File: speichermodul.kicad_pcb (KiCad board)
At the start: 2 copper layers, 100 x 160 mm, 65 parts, among them IC1 6116, P1 CONN_3X2, P2 CONN_01X01, P3 CONN_01X01, P4 CONN_01X01, P5 CONN_01X01, P6 CONN_01X01, P7 CONN_01X01, P8 CONN_02X10, P9 CONN_02X10, SW1 SW_PUSH, SW2 SW_PUSH, U1 7400, U2 74LS08, U3 74LS08, U4 74LS14, U5 74LS540, U6 74LS540

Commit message: mit Korrektur der Anordnung begonnen
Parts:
- removed REF**: EuroBoard160mmX100mm, EuroBoard_Outline:EuroBoard160mmX100mm
- removed REF***: KiCad-Logo2_30mm_SilkScreen, Symbols:KiCad-Logo2_30mm_SilkScreen
- removed RP3: R_PACK8BUSSED, Housings_SIP:SIP9_Housing_BigPads
- added RP2: R_PACK8BUSSED, Housings_SIP:SIP9_Housing_BigPads, F.Cu at (72.6, 66.8)
- D1, D2: footprint LEDs:LED-3MM -> LEDs:LED_D3.0mm
- P8: footprint Connect:IDC_Header_Straight_20pins -> Connectors_Samtec:SDL-120-X-XX_2x10
- R24, R25, R3: footprint Resistors_ThroughHole:R_Axial_DIN0207_L6.3mm_D2.5mm_P10.16mm_Horizontal -> Resistors_ThroughHole:R_Axial_DIN0309_L9.0mm_D3.2mm_P15.24mm_Horizontal
- SW1, SW2: footprint Buttons_Switches_ThroughHole:SW_PUSH_6mm_h5mm -> tg_foodprint:SW_PUSH_LCD_E3_SAxxxx_tg
- U5: footprint Housings_DIP:DIP-20_W7.62mm_LongPads -> Housings_DIP:DIP-20_W7.62mm_Socket_LongPads
- moved D18 104.1 mm to (57.1, 29.2)
- moved U5 99.1 mm to (64.8, 160.0)
- moved U6 99.1 mm to (62.2, 61.0)
- moved R16 95.3 mm to (57.1, 36.8)
- moved D10 51.9 mm to (5.84, 21.6)
- moved R4 48.8 mm to (8.38, 39.6)
- moved P8 34.9 mm to (152.1, 43.4)
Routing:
- net Net-(D10-Pad1): track 7.62 -> 0.00 mm
- net Net-(D11-Pad1): track 5.08 -> 10.2 mm
- net Net-(R4-Pad2): track 13.5 -> 17.7 mm
- net Net-(R16-Pad2): track 17.7 -> 13.5 mm
- net Net-(D18-Pad1): track 5.08 -> 7.62 mm
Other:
- board outline removed

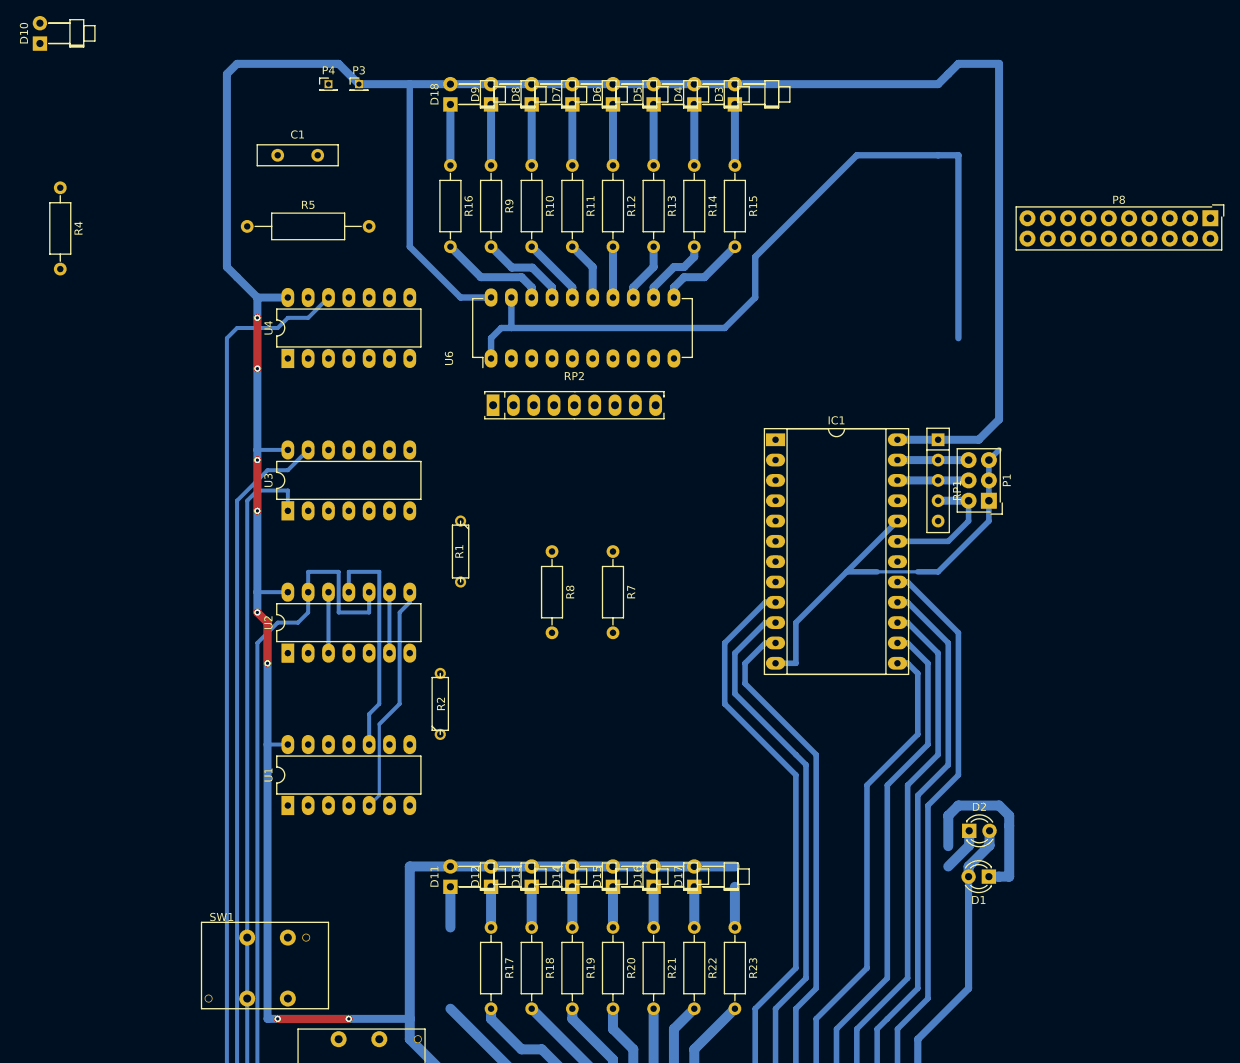
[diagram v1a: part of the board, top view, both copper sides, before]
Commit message: busses new arranged
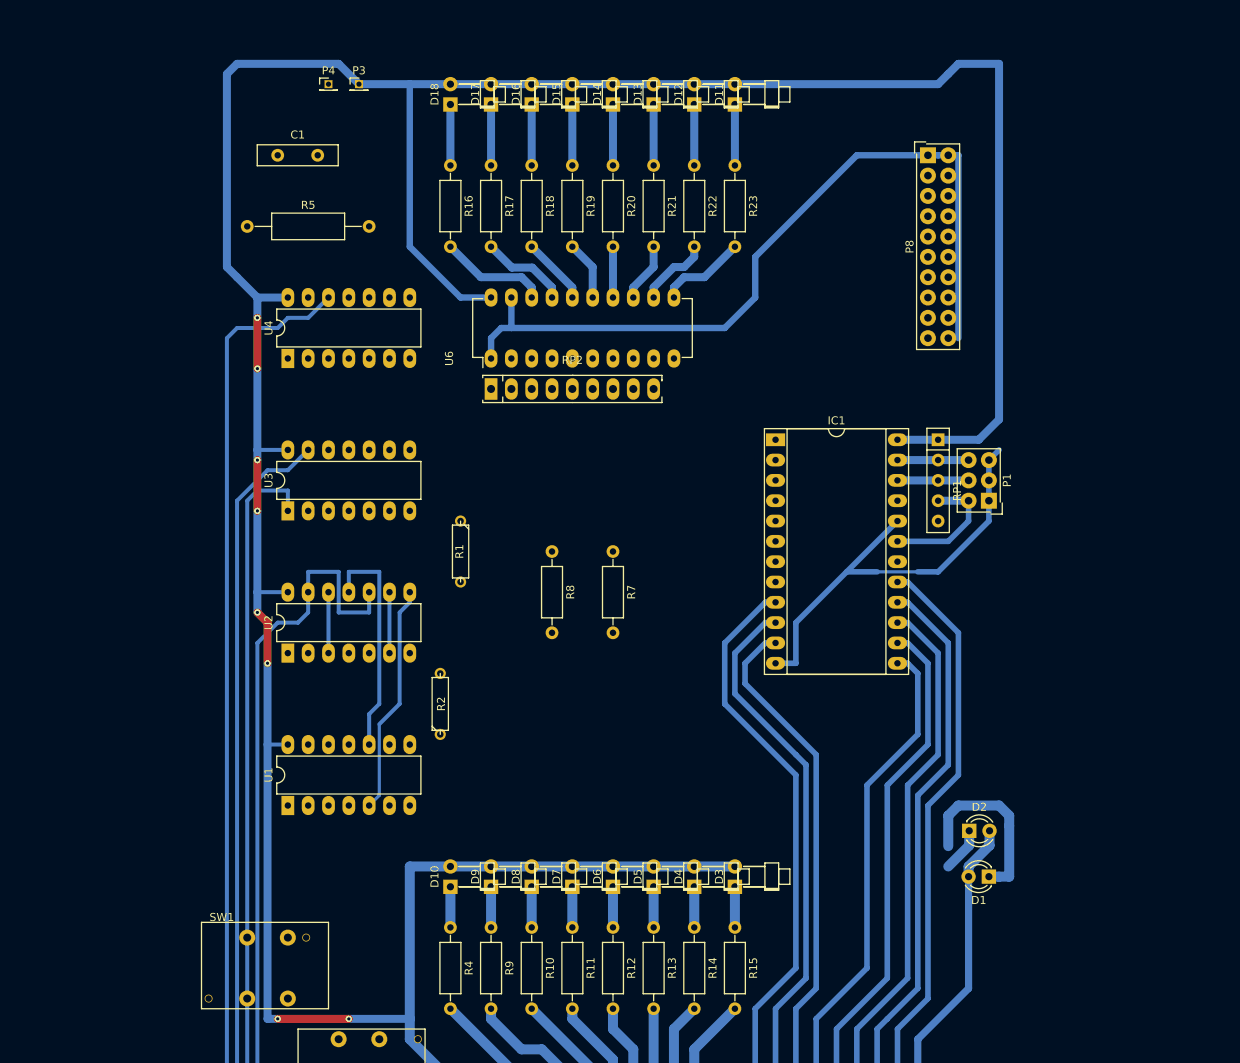
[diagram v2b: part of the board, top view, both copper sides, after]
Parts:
- moved D10 117.2 mm to (57.1, 127.0)
- moved R4 104.5 mm to (57.1, 132.1)
- moved D11 104.1 mm to (92.7, 29.2)
- moved D12 101.0 mm to (87.6, 29.2)
- moved D17 101.0 mm to (62.2, 29.2)
- moved D13 99.0 mm to (82.5, 29.2)
- moved D16 99.0 mm to (67.3, 29.2)
- moved D14 97.9 mm to (77.5, 29.2)
- moved D15 97.9 mm to (72.4, 29.2)
- moved D3 97.8 mm to (92.7, 127.0)
- moved D4 97.8 mm to (87.6, 127.0)
- moved D5 97.8 mm to (82.5, 127.0)
- moved D6 97.8 mm to (77.5, 127.0)
- moved D7 97.8 mm to (72.4, 127.0)
- moved D8 97.8 mm to (67.3, 127.0)
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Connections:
- IC1 pad 1: /A7 -> /A0
- IC1 pad 10: /D1 -> /D6
- IC1 pad 11: /D2 -> /D5
- IC1 pad 13: /D3 -> /D4
- IC1 pad 14: /D4 -> /D3
- IC1 pad 15: /D5 -> /D2
- IC1 pad 16: /D6 -> /D1
- IC1 pad 17: /D7 -> /D0
- IC1 pad 2: /A6 -> /A1
- IC1 pad 3: /A5 -> /A2
- IC1 pad 4: /A4 -> /A3
- IC1 pad 5: /A3 -> /A4
- IC1 pad 6: /A2 -> /A5
- IC1 pad 7: /A1 -> /A6
- IC1 pad 8: /A0 -> /A7
- IC1 pad 9: /D0 -> /D7
- P9 pad 11: /D3 -> /D4
- P9 pad 13: /D2 -> /D5
- P9 pad 15: /D1 -> /D6
- P9 pad 17: /D0 -> /D7
- P9 pad 3: /D7 -> /D0
- P9 pad 5: /D6 -> /D1
- P9 pad 7: /D5 -> /D2
- P9 pad 9: /D4 -> /D3
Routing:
- net Net-(D10-Pad1): track 0.00 -> 5.08 mm
- net Net-(R20-Pad2): track 11.2 -> 6.35 mm
- net Net-(R12-Pad2): track 6.35 -> 11.2 mm
- net Net-(R18-Pad2): track 13.3 -> 8.45 mm
- net Net-(R10-Pad2): track 8.45 -> 13.3 mm
- net Net-(R9-Pad2): track 11.0 -> 15.9 mm
- net Net-(R17-Pad2): track 15.9 -> 11.0 mm
- net Net-(R19-Pad2): track 12.3 -> 7.40 mm
- net Net-(R11-Pad2): track 7.40 -> 12.3 mm
- net Net-(R21-Pad2): track 10.2 -> 7.40 mm
- net Net-(R13-Pad2): track 7.40 -> 10.2 mm
- net Net-(D11-Pad1): track 10.2 -> 7.62 mm
- net /D4: track 85.8 -> 83.3 mm
- net /D3: track 83.3 -> 85.8 mm
- net Net-(D9-Pad1): track 7.62 -> 5.08 mm
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
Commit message: Pcb layout viel weitergebracht
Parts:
- moved C1 10.2 mm to (45.7, 35.6), turned to 90 degrees
- moved R8 9.67 mm to (73.7, 94.0)
- moved SW1 8.98 mm to (45.7, 132.1), turned to 270 degrees
- moved R7 8.89 mm to (77.5, 94.0)
- moved SW2 7.73 mm to (44.5, 146.1), turned to 0 degrees
- moved R2 6.84 mm to (58.4, 110.5)
- moved R1 2.54 mm to (61.0, 85.1)
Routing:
- net GND: track 311.2 -> 512.9 mm, vias 0 -> 7
- net Net-(IC1-Pad21): track 0.00 -> 109.8 mm
- net Net-(IC1-Pad18): track 0.00 -> 98.8 mm, vias 0 -> 2
- net /A7: track 0.00 -> 85.6 mm
- net /A5: track 0.00 -> 84.8 mm, vias 0 -> 2
- net /A3: track 0.00 -> 84.8 mm, vias 0 -> 2
- net /A0: track 0.00 -> 84.8 mm, vias 0 -> 2
- net /A6: track 0.00 -> 84.8 mm, vias 0 -> 2
- net /A4: track 0.00 -> 84.8 mm, vias 0 -> 2
- net /A1: track 0.00 -> 84.8 mm, vias 0 -> 2
- net /A2: track 0.00 -> 84.1 mm, vias 0 -> 2
- net Net-(U1-Pad6): track 0.00 -> 77.4 mm
- net Net-(R2-Pad1): track 0.00 -> 68.8 mm
- net Net-(U1-Pad4): track 0.00 -> 63.9 mm
- net Net-(R7-Pad1): track 0.00 -> 59.2 mm
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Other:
- net class Default: trace_width 0.8 -> 0.3

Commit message: Butttons Neu
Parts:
- moved R1 39.0 mm to (48.3, 121.9), turned to 180 degrees
- moved R2 32.0 mm to (47.0, 140.3), turned to 0 degrees
- moved SW2 6.48 mm to (45.7, 152.4), turned to 270 degrees
- moved SW1 3.86 mm to (45.1, 135.9)
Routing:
- net Net-(R2-Pad1): track 68.8 -> 15.0 mm
- net GND: track 512.9 -> 564.1 mm, vias 7 -> 9
- net VCC: track 445.4 -> 474.4 mm, vias 8 -> 6
- net Net-(R1-Pad2): track 32.1 -> 35.1 mm
- net /_auto: track 115.0 -> 115.8 mm
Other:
- net class Default: trace_width 0.3 -> 0.4

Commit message: Powerpins neu gemacht
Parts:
- removed P2, P3, P4, P5, P6, P7: CONN_01X01, Pin_Headers:Pin_Header_Straight_1x01_Pitch1.27mm
- added J1: 2PinTerminalBlocktg, 2PinTerminalBlocktg, F.Cu at (44.5, 17.8)
- added J2: 2PinTerminalBlocktg, 2PinTerminalBlocktg, F.Cu at (22.9, 165.1)
- added J3: 2PinTerminalBlocktg, 2PinTerminalBlocktg, F.Cu at (22.9, 153.7)
- C1: value 0 -> 100n
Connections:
- net /_auto renamed AUTO
- net Net-(P6-Pad1) renamed WR
- net Net-(P7-Pad1) renamed RD
- C1 pad 1: GND -> VCC
- C1 pad 2: Net-(C1-Pad2) -> GND
- R5 pad 1: Net-(C1-Pad2) -> Net-(R5-Pad1)
- SW1 pad 0: (no net) -> GND
- SW1 pad 1: Net-(R1-Pad2) -> Net-(SW1-Pad1)
- SW1 pad 2: GND -> Net-(R1-Pad2)
- SW2 pad 0: (no net) -> Net-(SW2-Pad0)
- SW2 pad 1: GND -> Net-(SW2-Pad1)
- SW2 pad 2: Net-(R2-Pad1) -> GND
- U4 pad 12: Net-(P5-Pad1) -> EN
- U4 pad 13: Net-(C1-Pad2) -> Net-(R5-Pad1)
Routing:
- net Net-(P5-Pad1): track 135.5 -> 0.00 mm
- net EN: track 0.00 -> 135.5 mm
- net GND: track 564.1 -> 589.5 mm

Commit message: PCb layout
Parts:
- added C2: 100n, tg_foodprint:yyDisc_D10.0mm_W2.5mm_P.00mm, F.Cu at (34.3, 93.3)
- added C3: 100n, tg_foodprint:yyDisc_D10.0mm_W2.5mm_P.00mm, F.Cu at (34.3, 76.2)
- added C4: 100n, tg_foodprint:yyDisc_D10.0mm_W2.5mm_P.00mm, F.Cu at (34.3, 113.0)
- added C5: 100n, tg_foodprint:yyDisc_D10.0mm_W2.5mm_P.00mm, F.Cu at (34.3, 55.9)
- added C6: 100n, Capacitors_ThroughHole:C_Disc_D10.0mm_W2.5mm_P5.00mm, F.Cu at (165.4, 13.7)
- added C7: 100n, Capacitors_ThroughHole:C_Disc_D10.0mm_W2.5mm_P5.00mm, F.Cu at (163.2, 20.8)
- added D36: D, Diodes_ThroughHole:D_DO-41_SOD81_P10.16mm_Horizontal, F.Cu at (139.7, 13.3)
- moved J3 6.35 mm to (22.9, 160.0), turned to 90 degrees
- moved J2 5.08 mm to (22.9, 170.2), turned to 270 degrees
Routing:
- net GND: track 589.5 -> 599.2 mm
- net VCC: track 474.4 -> 478.2 mm, vias 6 -> 7
- net Net-(U1-Pad4): track 63.9 -> 67.1 mm
- net WR: track 106.0 -> 108.3 mm
- net Net-(U1-Pad6): track 77.4 -> 79.5 mm

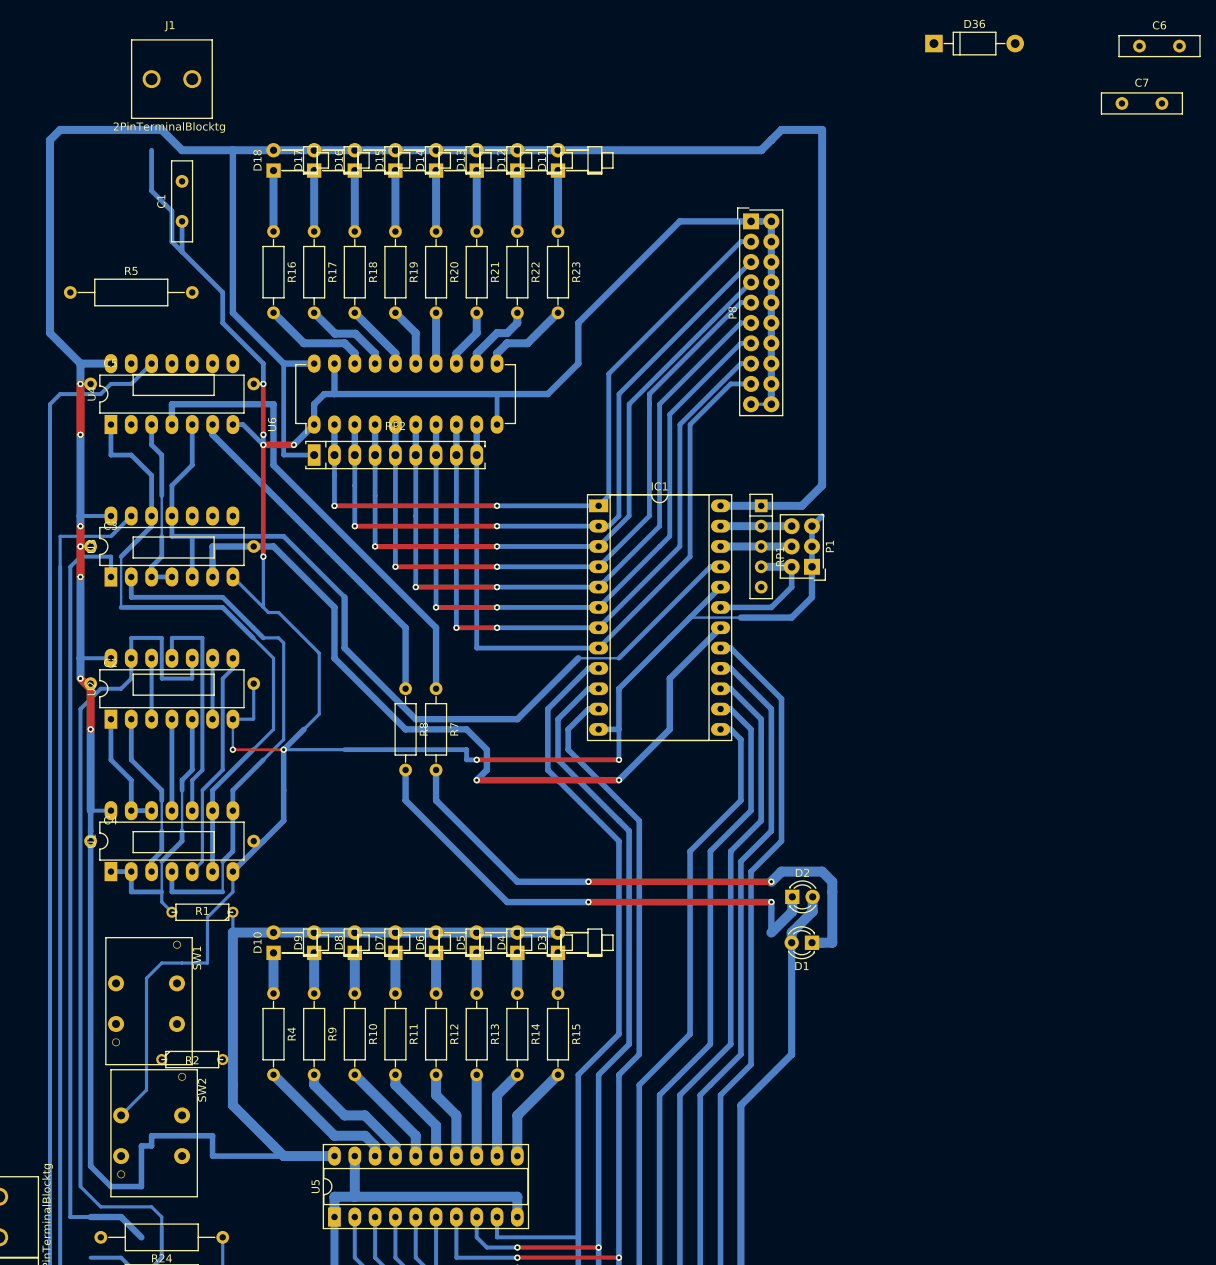
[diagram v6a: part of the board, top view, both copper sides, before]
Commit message: condensatoren eingefügt
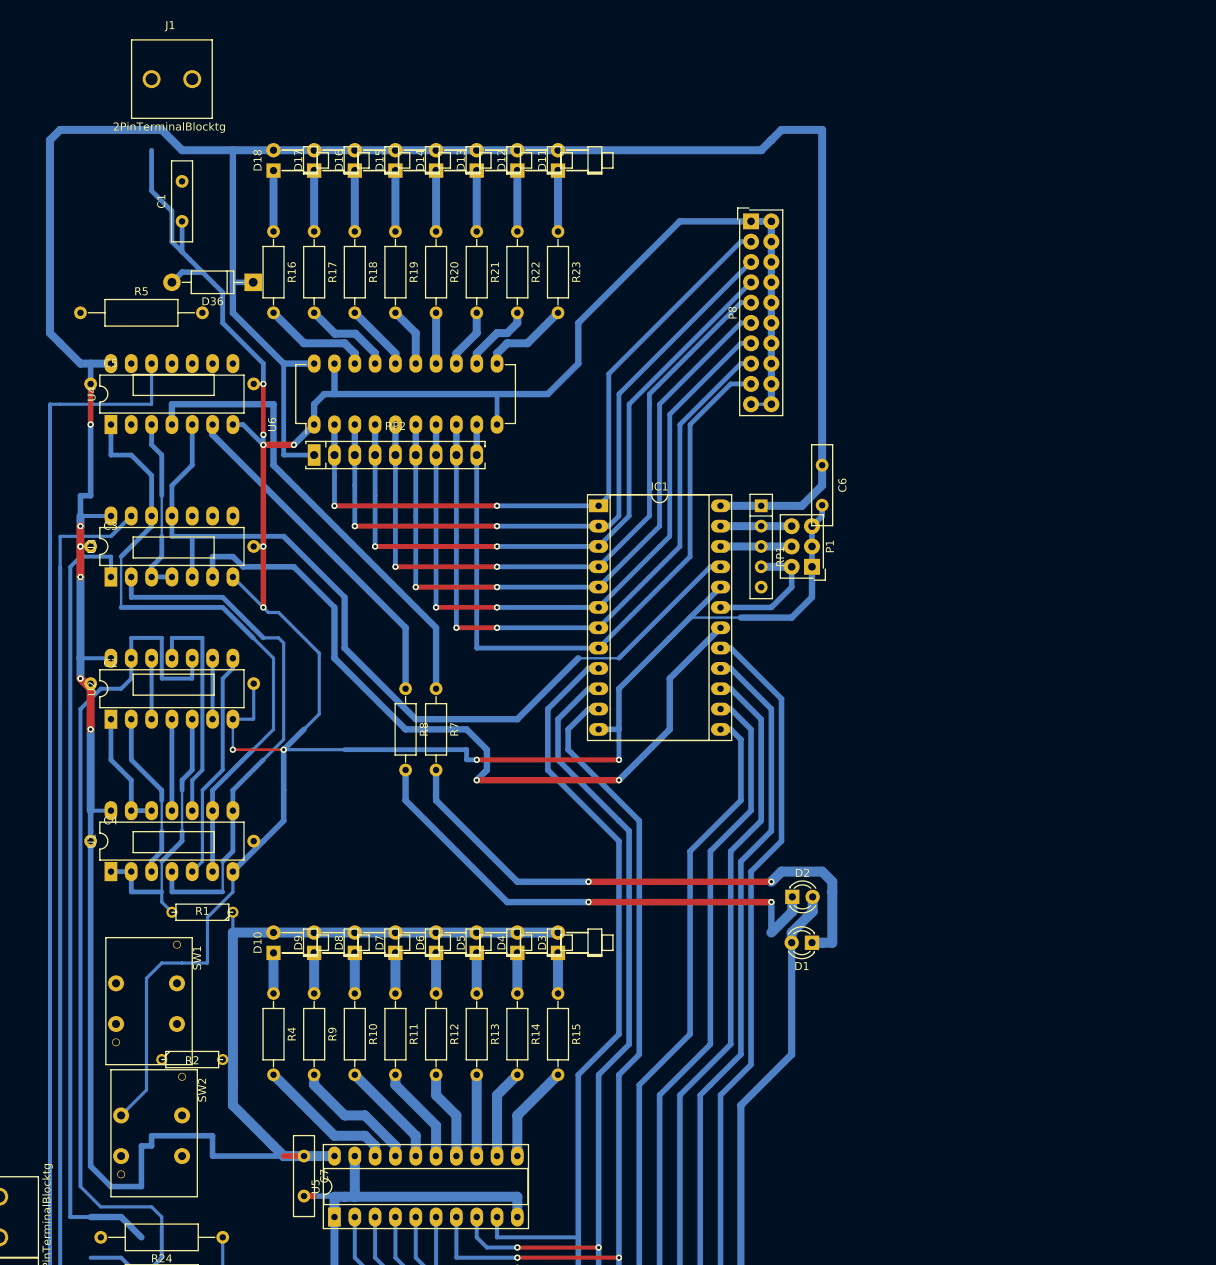
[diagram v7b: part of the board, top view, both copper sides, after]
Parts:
- moved C7 166.6 mm to (61.0, 152.4), turned to 270 degrees
- moved D36 90.2 mm to (54.6, 43.2), turned to 180 degrees
- moved C6 65.7 mm to (125.7, 66.0), turned to 270 degrees
- moved R5 2.84 mm to (33.0, 47.0)
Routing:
- net GND: track 599.2 -> 612.5 mm, vias 9 -> 10
- net VCC: track 478.2 -> 483.3 mm
- net EN: track 135.5 -> 138.4 mm
- net Net-(IC1-Pad18): track 98.8 -> 97.0 mm
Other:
- net class Default: trace_width 0.4 -> 0.7

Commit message: Letzte arbeit in der Stunde am 27.6.2018
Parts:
- removed R5: 0, Resistors_ThroughHole:R_Axial_DIN0309_L9.0mm_D3.2mm_P15.24mm_Horizontal
- added REF**: EuroBoard160mmX100mm_holes, EuroBoard_Outline:EuroBoard160mmX100mm_holes, F.Cu at (128.3, 182.9)
- added U7: 74LS08, Housings_DIP:DIP-14_W7.62mm_LongPads, F.Cu at (141.1, 13.4)
- moved J3 10.8 mm to (33.7, 160.0)
- moved J1 8.99 mm to (43.3, 26.7)
- moved J2 8.35 mm to (31.1, 171.4)
- moved C1 4.47 mm to (46.0, 31.1), turned to 270 degrees
- moved R24 1.91 mm to (52.7, 162.6)
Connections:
- SW2 pad 0: Net-(SW2-Pad0) -> Net-(R2-Pad1)
- U3 pad 10: (no net) -> GND
- U3 pad 8: (no net) -> Net-(U3-Pad8)
- U3 pad 9: (no net) -> GND
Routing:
- net GND: track 612.5 -> 635.0 mm
- net VCC: track 483.3 -> 488.1 mm
- net RD: track 99.4 -> 101.9 mm
- net Net-(R7-Pad1): track 59.2 -> 61.2 mm
- net AUTO: track 115.8 -> 117.3 mm
- net EN: track 138.4 -> 139.7 mm
- net WR: track 108.3 -> 109.2 mm
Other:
- board outline added: 100 x 160 mm
